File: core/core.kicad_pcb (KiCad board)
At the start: 4 copper layers, 30 x 50.9 mm, 97 parts, among them J1 Conn_01x03_Pin, J2 Conn_01x03_Pin, SW1 DS-THAM04-ABB-R, SW2 DS-THAM04-ABB-R, SW3 DS-THAM04-ABB-R, U1 F1C200S, U2 EA3036C, U3 XC6206P302MR_C347375, U4 CH340E, U5 W25Q128JVSIQTR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

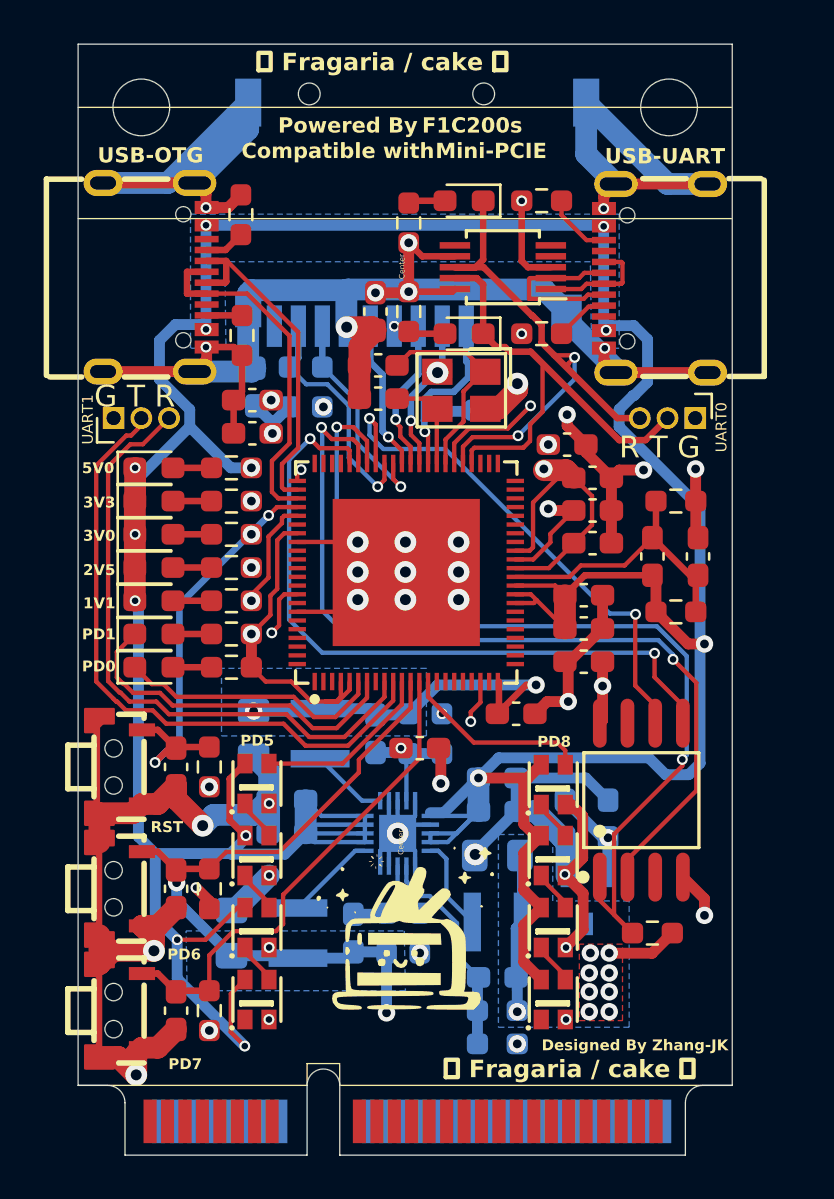
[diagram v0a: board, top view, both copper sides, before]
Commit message: delete all blind vias
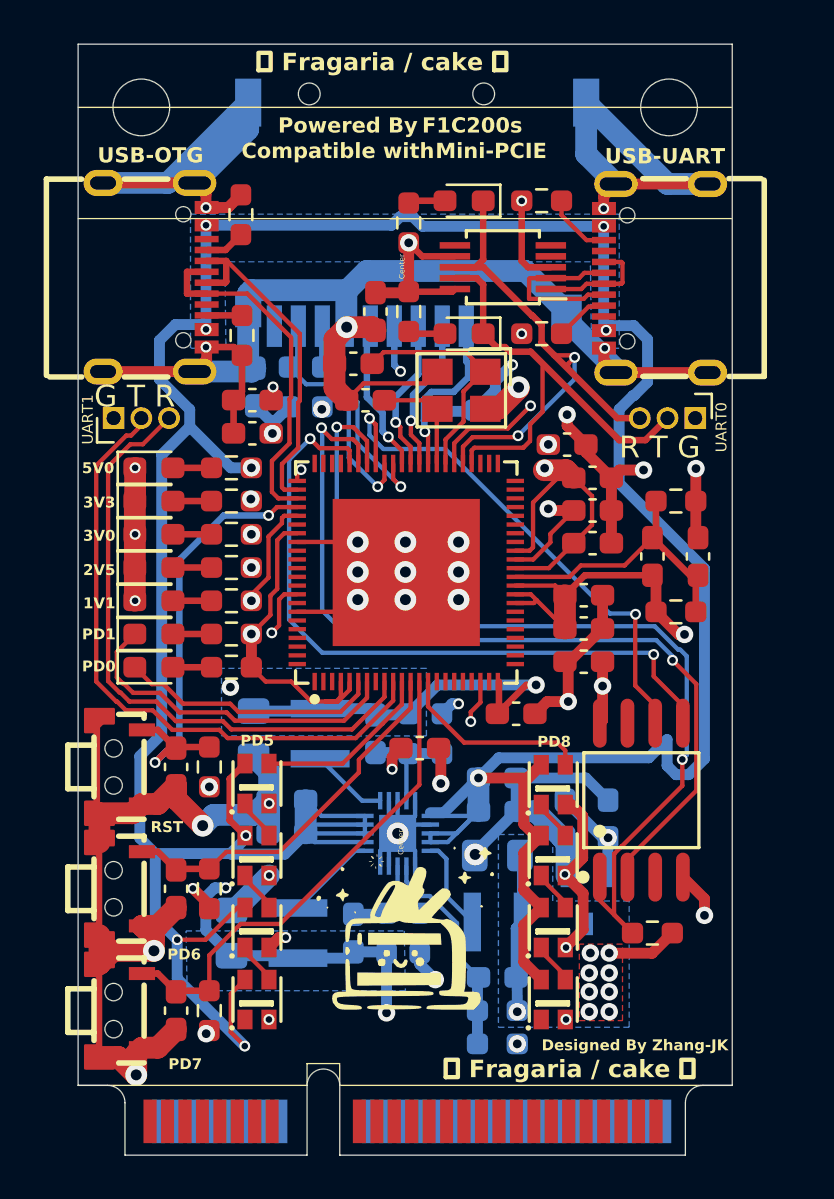
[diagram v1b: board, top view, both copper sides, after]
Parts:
- moved C15 1.15 mm to (195.1, 71.4)
- moved C14 0.59 mm to (195.6, 73.1)
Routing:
- net GND: track 201.5 -> 211.7 mm, vias 42 -> 41
- net +3V3: track 51.8 -> 56.9 mm, vias 28 -> 25
- net +5V: track 166.4 -> 168.2 mm
- net +1V1: track 57.7 -> 56.4 mm
- net /RESET: track 19.7 -> 20.9 mm
- net /HOSCI: track 9.69 -> 10.8 mm
- net /HOSCO: track 4.56 -> 5.11 mm

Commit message: minor bug fix
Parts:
- C19, C20: value 0.1nF -> 0.1uF
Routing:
- net +2V5: track 97.2 -> 99.4 mm
- net +5V: track 168.2 -> 166.9 mm
